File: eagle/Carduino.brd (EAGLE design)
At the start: 88 x 88 mm, 92 parts, among them IC1 DS3231M+TRL, IC2 FT232RL, IC3 SN74HCS596DR, IC4 SN74HCS596DR, IC5 SN74HCS596DR, IC6 SN74HCS596DR, IC7 NTMD4184PFR2G, IC8 ATTINY404-SSNR, IC9 MCP73831T-3ACI_OT, U1 BAT-HLD-012-SMT

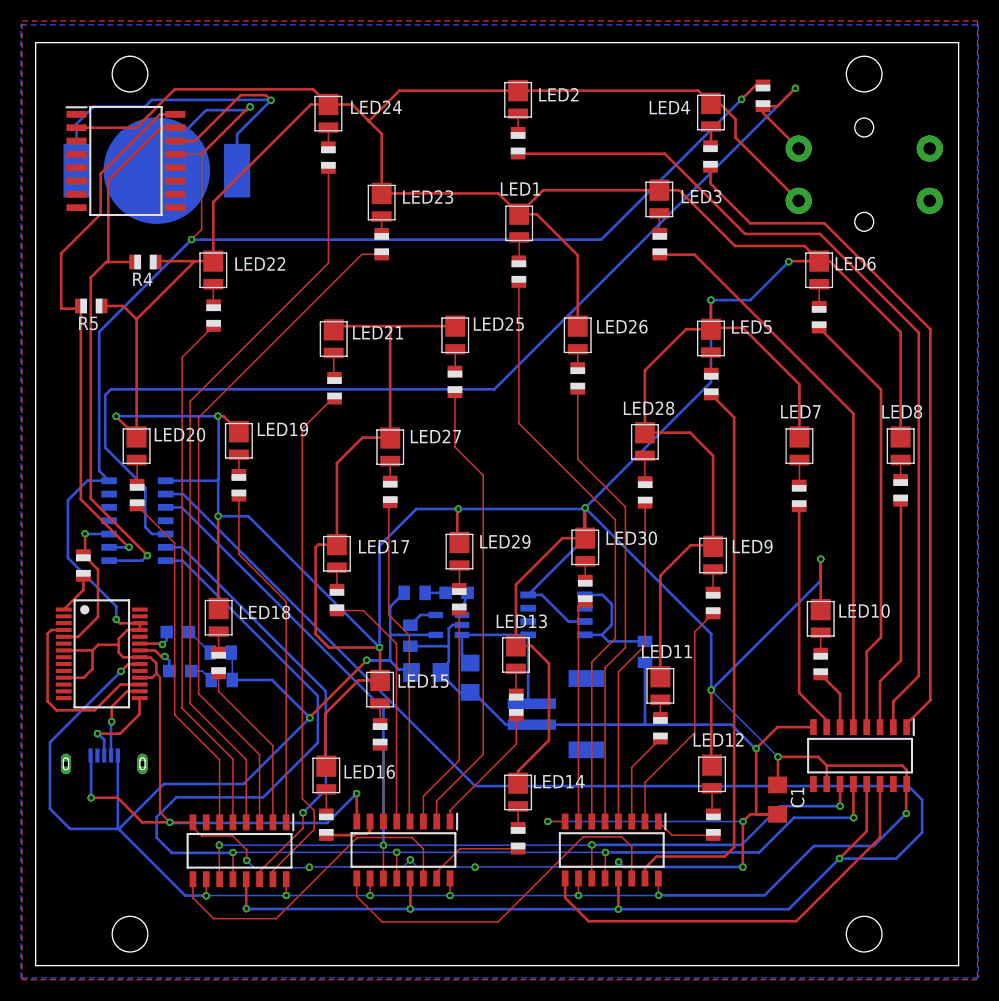
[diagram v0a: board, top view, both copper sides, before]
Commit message: removing dimensions that got into the board
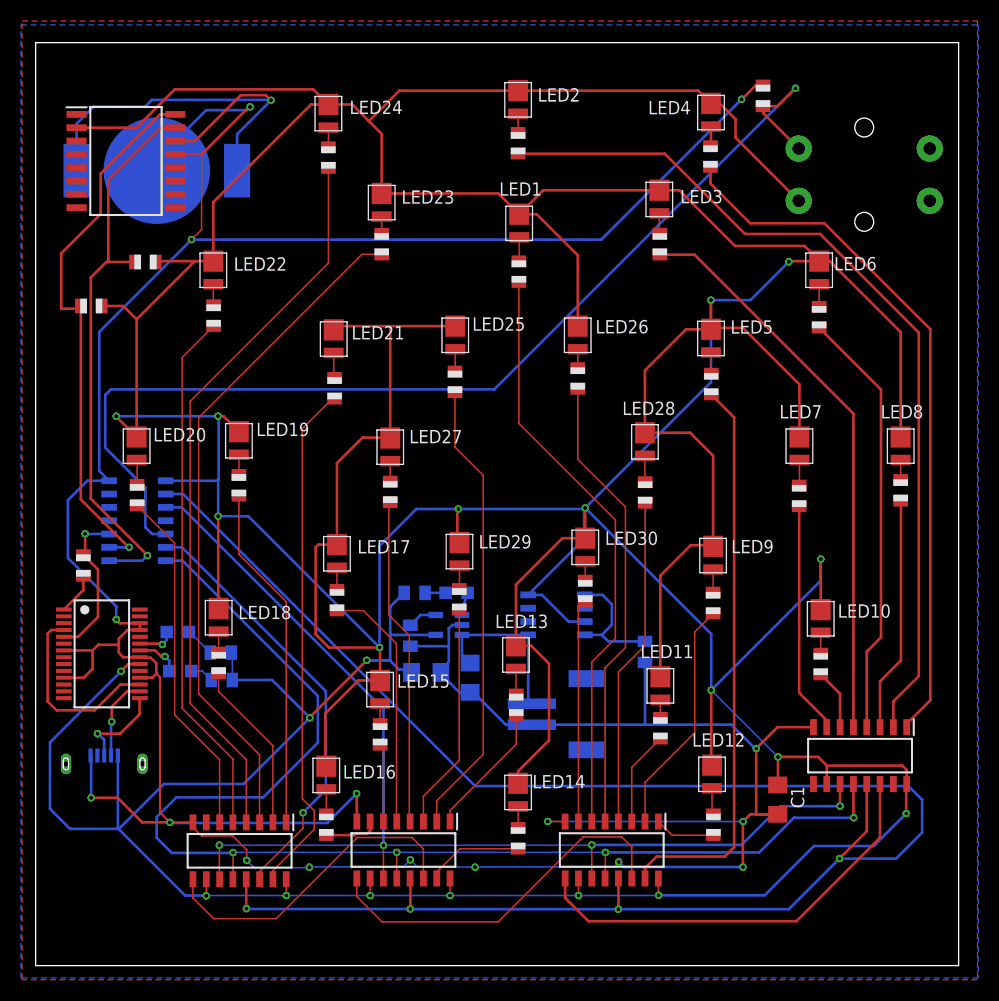
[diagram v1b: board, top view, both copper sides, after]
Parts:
- removed U$1, U$2, U$3, U$4: (no value), Pierre:M3HOLE
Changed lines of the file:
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@@
 <rectangle x1="50.9714" y1="67.3254" x2="51.2762" y2="67.3762" layer="200" rot="R180"/>
 <text x="0" y="-0.254" size="0.1016" layer="200" font="vector">C:/Users/pierr/Documents/Sparkle/vanillalogo.bmp</text>
-<dimension x1="8.39" y1="58.65" x2="83.52" y2="58.65" x3="45.955" y3="85.01" textsize="1.778" layer="1"/>
-<dimension x1="51.9" y1="84.61" x2="53.08" y2="9.65" x3="96.116496875" y3="47.81675625" textsize="1.778" layer="1"/>
 </plain>
 <attributes>
@@
 </element>
 <element name="R4" library="adafruit" package="R0805" value="4.7K" x="10.4648" y="67.0814" smashed="yes" rot="R180">
-<attribute name="NAME" x="11.2268" y="66.0654" size="1.27" layer="25" rot="R180"/>
 <attribute name="VALUE" x="11.2268" y="69.3674" size="1.27" layer="27" rot="R180"/>
 </element>
 <element name="R5" library="adafruit" package="R0805" value="4.7K" x="5.3086" y="62.8904" smashed="yes" rot="R180">
-<attribute name="NAME" x="6.0706" y="61.8744" size="1.27" layer="25" rot="R180"/>
 <attribute name="VALUE" x="6.0706" y="65.1764" size="1.27" layer="27" rot="R180"/>
 </element>
-<element name="U$1" library="Pierre" package="M3HOLE" value="" x="9" y="3" smashed="yes"/>
-<element name="U$2" library="Pierre" package="M3HOLE" value="" x="79" y="3" smashed="yes"/>
-<element name="U$3" library="Pierre" package="M3HOLE" value="" x="9" y="85" smashed="yes"/>
-<element name="U$4" library="Pierre" package="M3HOLE" value="" x="79" y="85" smashed="yes"/>
 <element name="U$5" library="USB" package="USB3140-30-0170-0-C" value="USB3140" x="6.54" y="20.03" smashed="yes" rot="MR0"/>
 <element name="S1" library="adafruit" library_urn="urn:adsk.eagle:library:420" package="B3F-40XX-ROUND" package3d_urn="urn:adsk.eagle:package:6240926/1" value="" x="79" y="75.41" smashed="yes" rot="MR0">
@@
 </element>
 <element name="CN1" library="adafruit" library_urn="urn:adsk.eagle:library:420" package="JST-PH-2-SMT-RA" package3d_urn="urn:adsk.eagle:package:6240692/1" value="" x="51.01" y="23.97" smashed="yes" rot="MR90">
-<attribute name="NAME" x="54.82" y="21.43" size="1.27" layer="26" font="vector" rot="MR90"/>
 <attribute name="VALUE" x="43.39" y="21.43" size="1.27" layer="28" font="vector" rot="MR90"/>
 </element>
@@
 </element>
 <element name="CHARGING" library="adafruit" package="CHIP-LED0805" value="Red" x="40.13" y="35.54" smashed="yes" rot="MR90">
-<attribute name="NAME" x="37.74" y="40.13" size="1.27" layer="26" rot="MR270"/>
+<attribute name="NAME" x="37.72" y="39.09" size="1.27" layer="26" rot="MR180"/>
 </element>
 <element name="R21" library="adafruit" package="R0805" value="100K" x="58.1" y="29.91" smashed="yes" rot="MR270">
-<attribute name="NAME" x="57.084" y="30.672" size="1.27" layer="26" rot="MR270"/>
-<attribute name="VALUE" x="60.386" y="30.672" size="1.27" layer="28" rot="MR270"/>
+<attribute name="VALUE" x="60.866" y="31.892" size="1.27" layer="28" rot="MR270"/>
 </element>
 <element name="R22" library="adafruit" package="R0805" value="10K" x="35.73" y="31.45" smashed="yes" rot="MR270">
-<attribute name="NAME" x="34.714" y="32.212" size="1.27" layer="26" rot="MR270"/>
-<attribute name="VALUE" x="38.016" y="32.212" size="1.27" layer="28" rot="MR270"/>
+<attribute name="VALUE" x="34.416" y="33.892" size="1.27" layer="28" rot="MR270"/>
 </element>
 <element name="C2" library="resistor" package="C1206" value="4.7uF" x="41.43" y="27.45" smashed="yes" rot="MR270">
@@
 </element>
 <element name="C3" library="resistor" package="C1206" value="1uF" x="37.24" y="27.95" smashed="yes" rot="MR0">
-<attribute name="NAME" x="38.51" y="29.22" size="1.27" layer="26" rot="MR0"/>
-<attribute name="VALUE" x="38.51" y="25.41" size="1.27" layer="28" rot="MR0"/>
+<attribute name="VALUE" x="38.73" y="25.23" size="1.27" layer="28" rot="MR0"/>
 </element>
 </elements>

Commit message: new clock and ftdi chips
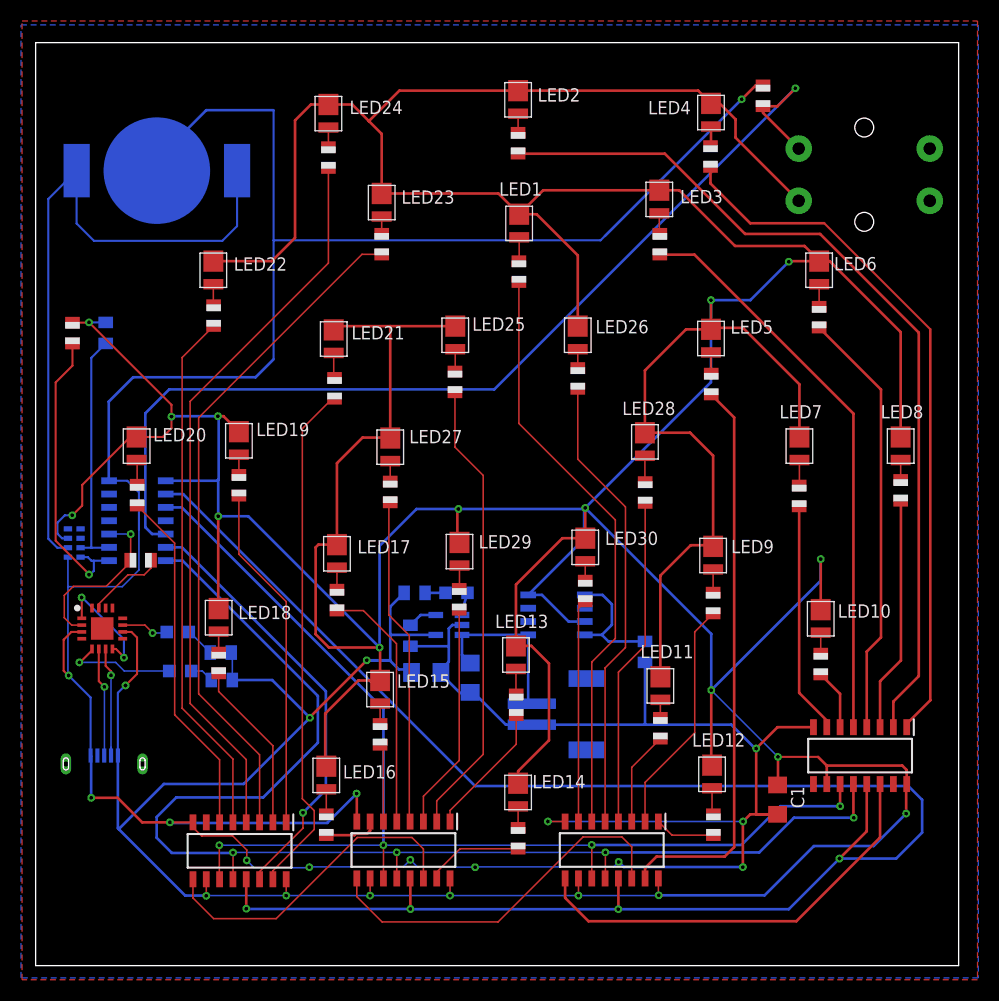
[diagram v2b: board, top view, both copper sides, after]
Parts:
- removed IC2: FT232RL, ftdichip:SSOP28
- removed R1: 470, adafruit:R0805
- added IC11: RV-3028-C7_32.768KHZ_1PPM_TA_Q, SamacSys_Parts:RV3028C732768KHZ1PPMTAQC
- added R23: 470, adafruit:R0805
- IC1: value DS3231M+TRL -> FT230XQ-R; device SamacSys_Parts:SOIC127P1032X265-16N -> SamacSys_Parts:QFN65P400X400X80-17N
- moved IC1 44.6 mm to (6.35, 32.1)
- moved R4 9.71 mm to (3.51, 60.3), turned to 270 degrees
- moved R5 2.91 mm to (6.68, 60.3), flipped to the bottom, turned to 270 degrees
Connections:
- removed net N$101: IC2.17, IC2.4
- removed net N$102: IC2.1, R1.1
- removed net N$107: IC2.22, RX.C
- new net N$41: IC1.15, R23.1
- new net N$42: IC1.1, IC1.8
- new net N$43: IC1.11, TX.C
- net GND: now also IC1.3, IC11.5; no longer IC1.13, IC2.11, IC2.18, IC2.21, IC2.25, IC2.26, IC2.7
- net N$100: now also IC1.6; no longer IC2.15
- net N$103: now also IC1.2, R23.2; no longer IC2.5, R1.2
- net N$106: now also IC1.5, RX.C; no longer IC2.23, TX.C
- net N$31: now also IC11.4; no longer IC1.15
- net N$32: now also IC11.3; no longer IC1.16
- net N$33: now also IC11.6; no longer IC1.14
- net N$99: now also IC1.7; no longer IC2.16
- net VCC: now also IC1.10, IC11.7; no longer IC1.2, IC2.20
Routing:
- net VCC: track 793.2 -> 756.7 mm, vias 21 -> 23
- net N$32: track 52.7 -> 22.8 mm, vias 1 -> 0
- net N$31: track 53.7 -> 28.5 mm
- net N$33: track 43.1 -> 65.3 mm, vias 1 -> 0
- net N$101: track 18.3 -> 0.00 mm
- net GND: track 358.1 -> 343.6 mm, vias 16 -> 14
- net N$42: track 0.00 -> 10.9 mm, vias 0 -> 2
- net N$41: track 0.00 -> 7.53 mm
- net N$106: track 3.57 -> 10.7 mm
- net N$34: track 103.6 -> 97.1 mm
- net N$43: track 0.00 -> 4.57 mm, vias 0 -> 1
- net N$107: track 4.18 -> 0.00 mm, vias 1 -> 0
- net N$102: track 3.97 -> 0.00 mm
- net N$99: track 7.97 -> 10.4 mm
- net N$103: track 14.9 -> 16.7 mm
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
